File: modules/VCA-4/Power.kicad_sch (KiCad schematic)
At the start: 33 parts, among them J17 Conn_Eurorack_10, U1 LM4040, U2 SSI2164, U3 TL074, U4 TL074, U5 TL074, U6 TL074

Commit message: VCA-4: wip
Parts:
- removed R2: 150K, -lmp-misc:R_Axial_DIN0207_L6.3mm_D2.5mm_P7.62mm_Horizontal, symbol -lmp:R_1%_0W166
- removed R3: 100K, -lmp-misc:R_Axial_DIN0207_L6.3mm_D2.5mm_P7.62mm_Horizontal, symbol -lmp:R_1%_0W166
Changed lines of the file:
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@@
   (junction (at 67.31 107.95) (diameter 0) (color 0 0 0 0)
   )
-  (junction (at 78.74 49.53) (diameter 0) (color 0 0 0 0)
-  )
   (junction (at 57.15 57.15) (diameter 0) (color 0 0 0 0)
   )
@@
   (junction (at 92.71 107.95) (diameter 0) (color 0 0 0 0)
   )
-  (junction (at 87.63 41.91) (diameter 0) (color 0 0 0 0)
-  )
-  (junction (at 102.87 41.91) (diameter 0) (color 0 0 0 0)
-  )
   (junction (at 57.15 41.91) (diameter 0) (color 0 0 0 0)
   )
@@
     (stroke (width 0) (type default) (color 0 0 0 0))
   )
-  (wire (pts (xy 87.63 41.91) (xy 93.98 41.91))
-    (stroke (width 0) (type default) (color 0 0 0 0))
-  )
   (wire (pts (xy 199.39 102.87) (xy 204.47 102.87))
     (stroke (width 0) (type default) (color 0 0 0 0))
@@
     (stroke (width 0) (type default) (color 0 0 0 0))
   )
-  (wire (pts (xy 102.87 41.91) (xy 102.87 39.37))
-    (stroke (width 0) (type default) (color 0 0 0 0))
-  )
   (wire (pts (xy 140.97 107.95) (xy 163.83 107.95))
     (stroke (width 0) (type default) (color 0 0 0 0))
@@
     (stroke (width 0) (type default) (color 0 0 0 0))
   )
-  (wire (pts (xy 102.87 39.37) (xy 104.14 39.37))
-    (stroke (width 0) (type default) (color 0 0 0 0))
-  )
   (wire (pts (xy 139.7 105.41) (xy 140.97 105.41))
     (stroke (width 0) (type default) (color 0 0 0 0))
@@
     (stroke (width 0) (type default) (color 0 0 0 0))
   )
-  (wire (pts (xy 78.74 49.53) (xy 102.87 49.53))
-    (stroke (width 0) (type default) (color 0 0 0 0))
-  )
   (wire (pts (xy 57.15 41.91) (xy 63.5 41.91))
     (stroke (width 0) (type default) (color 0 0 0 0))
@@
   )
   (wire (pts (xy 38.1 46.99) (xy 38.1 49.53))
-    (stroke (width 0) (type default) (color 0 0 0 0))
-  )
-  (wire (pts (xy 102.87 41.91) (xy 101.6 41.91))
     (stroke (width 0) (type default) (color 0 0 0 0))
   )
@@
   (text "Hardware" (at 161.29 27.94 0)
     (effects (font (size 1.27 1.27) (thickness 0.254) bold) (justify left bottom))
-  )
-  (global_label "+2VREF" (shape output) (at 104.14 39.37 0) (fields_autoplaced)
-    (effects (font (size 1.27 1.27)) (justify left))
-    (property "Intersheet References" "${INTERSHEET_REFS}" (id 0) (at 1.27 0 0)
-      (effects (font (size 1.27 1.27)) hide)
-    )
   )
   (symbol (lib_id "-lmp-synth:Conn_Eurorack_Pwr_10") (at 43.18 46.99 0) (unit 1)
@@
     (pin "2")
   )
-  (symbol (lib_id "-lmp:R_1%_0W166") (at 102.87 45.72 0) (unit 1)
-    (in_bom yes) (on_board yes)
-    (property "Reference" "R3" (id 0) (at 104.648 44.5516 0)
-      (effects (font (size 1.27 1.27)) (justify left))
-    )
-    (property "Value" "100K" (id 1) (at 104.648 46.863 0)
-      (effects (font (size 1.27 1.27)) (justify left))
-    )
-    (property "Footprint" "-lmp-misc:R_Axial_DIN0207_L6.3mm_D2.5mm_P7.62mm_Horizontal" (id 2) (at 101.092 45.72 90)
-      (effects (font (size 1.27 1.27)) hide)
-    )
-    (property "Datasheet" "https://www.mouser.ca/datasheet/2/447/Yageo_LR_MFR_1-1714151.pdf" (id 3) (at 102.87 45.72 0)
-      (effects (font (size 1.27 1.27)) hide)
-    )
-    (property "Manufacturer" "YAGEO" (id 4) (at 102.87 45.72 0)
-      (effects (font (size 1.27 1.27)) hide)
-    )
-    (property "ManufacturerPartNum" "MFR-12*" (id 5) (at 102.87 45.72 0)
-      (effects (font (size 1.27 1.27)) hide)
-    )
-    (property "Distributor" "Mouser" (id 6) (at 102.87 45.72 0)
-      (effects (font (size 1.27 1.27)) hide)
-    )
-    (property "DistributorPartNum" "603-MFR-12*" (id 7) (at 102.87 45.72 0)
-      (effects (font (size 1.27 1.27)) hide)
-    )
-    (property "DistributorPartLink" "https://www.mouser.ca/c/?m=YAGEO&power+rating=166+mW+(1%2f6+W)&tolerance=1+%25&instock=y" (id 8) (at 102.87 45.72 0)
-      (effects (font (size 1.27 1.27)) hide)
-    )
-    (property "Value2" "1%, 1/6 W" (id 9) (at 107.823 45.72 90)
-      (effects (font (size 1.27 1.27)) hide)
-    )
-    (pin "1")
-    (pin "2")
-  )
   (symbol (lib_id "-lmp:R_1%_0W166") (at 72.39 41.91 270) (unit 1)
     (in_bom yes) (on_board yes)
@@
       (effects (font (size 1.27 1.27)) hide)
     )
-    (pin "1")
-    (pin "2")
-  )
-  (symbol (lib_id "-lmp:R_1%_0W166") (at 97.79 41.91 270) (unit 1)
-    (in_bom yes) (on_board yes)
-    (property "Reference" "R2" (id 0) (at 97.79 36.6522 90))
-    (property "Value" "150K" (id 1) (at 97.79 38.9636 90))
-    (property "Footprint" "-lmp-misc:R_Axial_DIN0207_L6.3mm_D2.5mm_P7.62mm_Horizontal" (id 2) (at 97.79 40.132 90)
-      (effects (font (size 1.27 1.27)) hide)
-    )
-    (property "Datasheet" "https://www.mouser.ca/datasheet/2/447/Yageo_LR_MFR_1-1714151.pdf" (id 3) (at 97.79 41.91 0)
-      (effects (font (size 1.27 1.27)) hide)
-    )
-    (property "Manufacturer" "YAGEO" (id 4) (at 97.79 41.91 0)
-      (effects (font (size 1.27 1.27)) hide)
-    )
-    (property "ManufacturerPartNum" "MFR-12*" (id 5) (at 97.79 41.91 0)
-      (effects (font (size 1.27 1.27)) hide)
-    )
-    (property "Distributor" "Mouser" (id 6) (at 97.79 41.91 0)
-      (effects (font (size 1.27 1.27)) hide)
-    )
-    (property "DistributorPartNum" "603-MFR-12*" (id 7) (at 97.79 41.91 0)
-      (effects (font (size 1.27 1.27)) hide)
-    )
-    (property "DistributorPartLink" "https://www.mouser.ca/c/?m=YAGEO&power+rating=166+mW+(1%2f6+W)&tolerance=1+%25&instock=y" (id 8) (at 97.79 41.91 0)
-      (effects (font (size 1.27 1.27)) hide)
-    )
-    (property "Value2" "1%, 1/6 W" (id 9) (at 97.79 46.863 90)
-      (effects (font (size 1.27 1.27)) hide)
-    )

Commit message: VCA-4: wip
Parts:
- U2: footprint -lmp-breakout:Breakout_DIP-16_W15.24mm -> -lmp-breakout:Breakout_DIP-SOIC-16_W15.24mm
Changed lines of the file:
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@@
       (effects (font (size 1.27 1.27)) (justify left))
     )
-    (property "Footprint" "-lmp-breakout:Breakout_DIP-16_W15.24mm" (id 2) (at 149.86 111.76 0)
+    (property "Footprint" "-lmp-breakout:Breakout_DIP-SOIC-16_W15.24mm" (id 2) (at 149.86 111.76 0)
       (effects (font (size 1.27 1.27)) hide)
     )

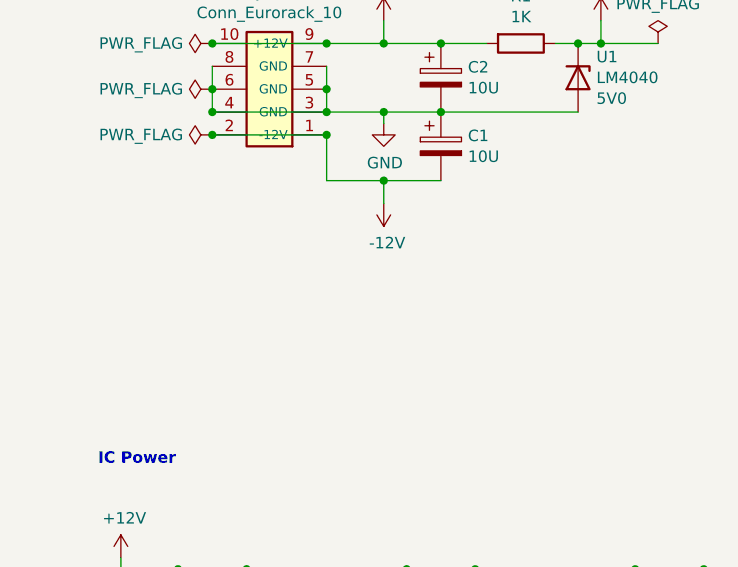
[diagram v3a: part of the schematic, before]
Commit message: VCA4: Add Eurorack power cable to BOM
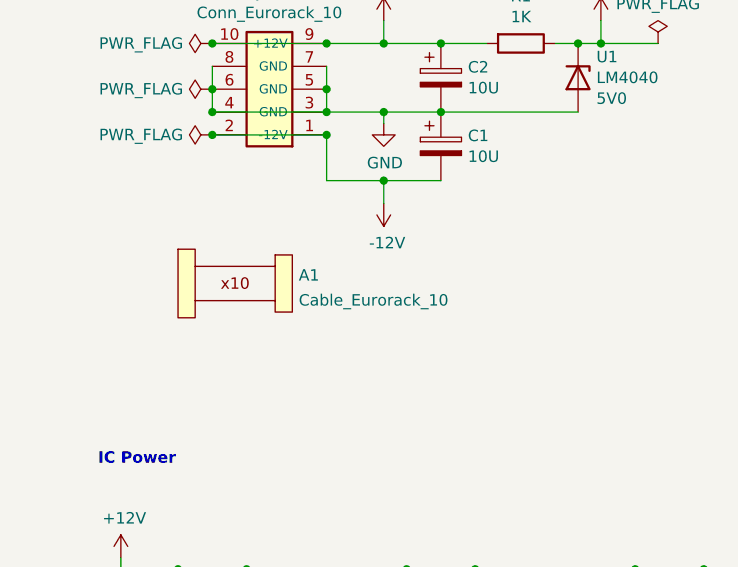
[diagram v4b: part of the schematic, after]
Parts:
- added A1: Cable_Eurorack_10, -lmp-misc:NoFootprint, symbol -lmp-synth:Cable_Eurorack_10
- U3, U4, U5, U6: footprint -lmp-misc:DIP-14_W7.62mm_LongPads -> Package_DIP:DIP-14_W7.62mm
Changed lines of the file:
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@@
       (effects (font (size 1.27 1.27)) (justify left))
     )
-    (property "Footprint" "-lmp-misc:DIP-14_W7.62mm_LongPads" (id 2) (at 35.56 105.41 0)
+    (property "Footprint" "Package_DIP:DIP-14_W7.62mm" (id 2) (at 35.56 105.41 0)
       (effects (font (size 1.27 1.27)) hide)
     )
@@
       (effects (font (size 1.27 1.27)) (justify left))
     )
-    (property "Footprint" "-lmp-misc:DIP-14_W7.62mm_LongPads" (id 2) (at 60.96 105.41 0)
+    (property "Footprint" "Package_DIP:DIP-14_W7.62mm" (id 2) (at 60.96 105.41 0)
       (effects (font (size 1.27 1.27)) hide)
     )
@@
       (effects (font (size 1.27 1.27)) (justify left))
     )
-    (property "Footprint" "-lmp-misc:DIP-14_W7.62mm_LongPads" (id 2) (at 86.36 105.41 0)
+    (property "Footprint" "Package_DIP:DIP-14_W7.62mm" (id 2) (at 86.36 105.41 0)
       (effects (font (size 1.27 1.27)) hide)
     )
@@
     (property "Reference" "U6" (id 0) (at 212.09 96.0882 0))
     (property "Value" "TL074" (id 1) (at 212.09 98.3996 0))
-    (property "Footprint" "-lmp-misc:DIP-14_W7.62mm_LongPads" (id 2) (at 210.82 102.87 0)
+    (property "Footprint" "Package_DIP:DIP-14_W7.62mm" (id 2) (at 210.82 102.87 0)
       (effects (font (size 1.27 1.27)) hide)
     )
@@
       (effects (font (size 1.27 1.27)) (justify left))
     )
-    (property "Footprint" "-lmp-misc:DIP-14_W7.62mm_LongPads" (id 2) (at 111.76 105.41 0)
+    (property "Footprint" "Package_DIP:DIP-14_W7.62mm" (id 2) (at 111.76 105.41 0)
       (effects (font (size 1.27 1.27)) hide)
     )
@@
     (pin "2")
   )
+  (symbol (lib_id "-lmp-synth:Cable_Eurorack_10") (at 40.64 68.58 0) (unit 1)
+    (in_bom yes) (on_board no) (fields_autoplaced)
+    (property "Reference" "A1" (id 0) (at 47.7012 67.6715 0)
+      (effects (font (size 1.27 1.27)) (justify left))
+    )
+    (property "Value" "Cable_Eurorack_10" (id 1) (at 47.7012 70.4466 0)
+      (effects (font (size 1.27 1.27)) (justify left))
+    )
+    (property "Footprint" "-lmp-misc:NoFootprint" (id 2) (at 41.275 73.66 0)
+      (effects (font (size 1.27 1.27)) hide)
+    )
+    (property "Datasheet" "" (id 3) (at 40.64 60.325 0)
+      (effects (font (size 1.27 1.27)) hide)
+    )
+    (property "Note" "Length as required" (id 4) (at 40.64 71.12 0)
+      (effects (font (size 1.27 1.27)) hide)
+    )
+    (property "Distributor" "Thonk" (id 5) (at 40.64 73.66 0)
+      (effects (font (size 1.27 1.27)) hide)
+    )
+    (property "DistributorPartLink" "https://www.thonk.co.uk/shop/eurorack-power-cables/" (id 6) (at 40.64 73.66 0)
+      (effects (font (size 1.27 1.27)) hide)
+    )
+    (property "Distributor2" "SynthCube" (id 7) (at 40.64 73.66 0)
+      (effects (font (size 1.27 1.27)) hide)
+    )
+    (property "DistributorPartLink2" "https://synthcube.com/cart/eurorack-ribbon-power-cables" (id 8) (at 40.64 73.66 0)
+      (effects (font (size 1.27 1.27)) hide)
+    )
+    (property "Distributor3" "Modular Addict" (id 9) (at 40.64 73.66 0)
+      (effects (font (size 1.27 1.27)) hide)
+    )
+    (property "DistributorPartLink3" "https://modularaddict.com/parts/eurorack-power-cables-1" (id 10) (at 40.64 73.66 0)
+      (effects (font (size 1.27 1.27)) hide)
+    )
+  )
   (symbol (lib_id "-lmp-synth:HW_Standoff_F-F_11mm_M3x0.50") (at 203.2 49.53 0) (unit 1)

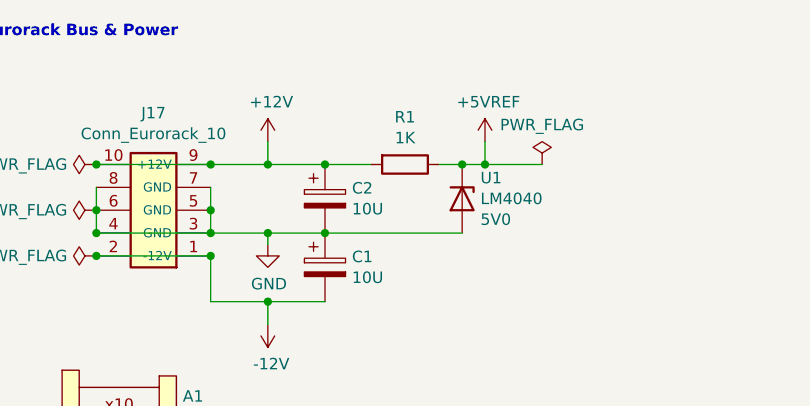
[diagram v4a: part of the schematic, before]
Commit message: VCA-4: BOM cleanup
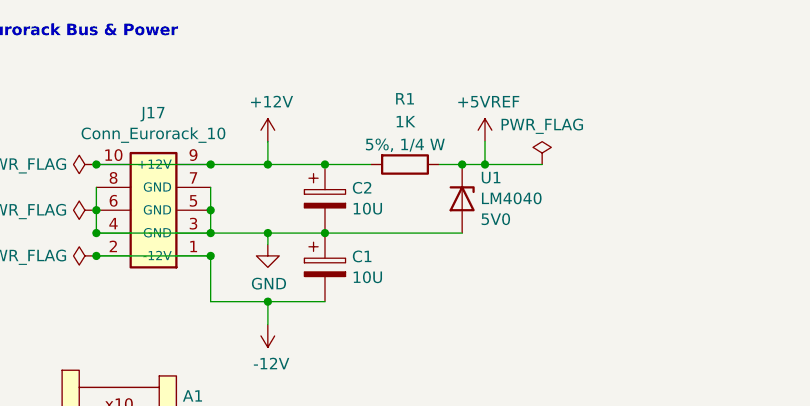
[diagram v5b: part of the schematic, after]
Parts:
- R1: footprint -lmp-misc:R_Axial_DIN0207_L6.3mm_D2.5mm_P7.62mm_Horizontal -> -lmp-misc:R_Axial_DIN0207_L6.3mm_D2.5mm_P10.16mm_Horizontal; symbol -lmp:R_1%_0W166 -> -lmp-synth:R_1K_Output; DistributorPartLink https://www.mouser.ca/c/?m=YAGEO&power+rating=166+mW+(1%2f6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 -> https://www.mouser.ca/ProductDetail/Vishay-Dale/CCF071K00JK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; DistributorPartNum 603-MFR-12* -> 71-CCF071K00JKE36; Manufacturer YAGEO -> Vishay / Dale; ManufacturerPartNum MFR-12* -> CCF071K00JKE36; Note (none) -> Output limiting; Value2 1%, 1/6 W -> 5%, 1/4 W
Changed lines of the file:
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@@
     (pin "2")
   )
-  (symbol (lib_id "-lmp:R_1%_0W166") (at 72.39 41.91 270) (unit 1)
-    (in_bom yes) (on_board yes)
-    (property "Reference" "R1" (id 0) (at 72.39 36.6522 90))
-    (property "Value" "1K" (id 1) (at 72.39 38.9636 90))
-    (property "Footprint" "-lmp-misc:R_Axial_DIN0207_L6.3mm_D2.5mm_P7.62mm_Horizontal" (id 2) (at 72.39 40.132 90)
+  (symbol (lib_id "-lmp-synth:R_1K_Output") (at 72.39 41.91 270) (unit 1)
+    (in_bom yes) (on_board yes) (fields_autoplaced)
+    (property "Reference" "R1" (id 0) (at 72.39 34.6574 90))
+    (property "Value" "1K" (id 1) (at 72.39 37.1943 90))
+    (property "Footprint" "-lmp-misc:R_Axial_DIN0207_L6.3mm_D2.5mm_P10.16mm_Horizontal" (id 2) (at 72.39 40.132 90)
       (effects (font (size 1.27 1.27)) hide)
     )
-    (property "Datasheet" "https://www.mouser.ca/datasheet/2/447/Yageo_LR_MFR_1-1714151.pdf" (id 3) (at 72.39 41.91 0)
+    (property "Datasheet" "https://www.mouser.ca/datasheet/2/427/ccf07-1762725.pdf" (id 3) (at 72.39 41.91 0)
       (effects (font (size 1.27 1.27)) hide)
     )
-    (property "Manufacturer" "YAGEO" (id 4) (at 72.39 41.91 0)
+    (property "Manufacturer" "Vishay / Dale" (id 4) (at 72.39 41.91 0)
       (effects (font (size 1.27 1.27)) hide)
     )
-    (property "ManufacturerPartNum" "MFR-12*" (id 5) (at 72.39 41.91 0)
+    (property "ManufacturerPartNum" "CCF071K00JKE36" (id 5) (at 72.39 41.91 0)
       (effects (font (size 1.27 1.27)) hide)
     )
-    (property "Distributor" "Mouser" (id 6) (at 72.39 41.91 0)
+    (property "Distributor" "Mouser" (id 6) (at 72.39 40.005 90)
       (effects (font (size 1.27 1.27)) hide)
     )
-    (property "DistributorPartNum" "603-MFR-12*" (id 7) (at 72.39 41.91 0)
+    (property "DistributorPartNum" "71-CCF071K00JKE36" (id 7) (at 72.39 41.91 0)
       (effects (font (size 1.27 1.27)) hide)
     )
-    (property "DistributorPartLink" "https://www.mouser.ca/c/?m=YAGEO&power+rating=166+mW+(1%2f6+W)&tolerance=1+%25&instock=y" (id 8) (at 72.39 41.91 0)
+    (property "DistributorPartLink" "https://www.mouser.ca/ProductDetail/Vishay-Dale/CCF071K00JKE36?qs=sGAEpiMZZMsPqMdJzcrNwqw41JD0NFylHV1MADcQnpo%3D" (id 8) (at 72.39 41.91 0)
       (effects (font (size 1.27 1.27)) hide)
     )
-    (property "Value2" "1%, 1/6 W" (id 9) (at 72.39 46.863 90)
+    (property "Value2" "5%, 1/4 W" (id 9) (at 72.39 39.7312 90))
+    (property "Note" "Output limiting" (id 10) (at 70.485 40.005 90)
       (effects (font (size 1.27 1.27)) hide)
     )

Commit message: VCA-4: PCB tweaks
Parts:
- C1, C2: footprint -lmp-misc:CP_Radial_D5.0mm_P2.50mm -> -lmp-misc:CP_Radial_D4.0mm_P1.50mm
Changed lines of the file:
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@@
       (effects (font (size 1.27 1.27)) (justify left))
     )
-    (property "Footprint" "-lmp-misc:CP_Radial_D5.0mm_P2.50mm" (id 2) (at 64.4652 49.53 0)
+    (property "Footprint" "-lmp-misc:CP_Radial_D4.0mm_P1.50mm" (id 2) (at 64.4652 49.53 0)
       (effects (font (size 1.27 1.27)) hide)
     )
@@
       (effects (font (size 1.27 1.27)) (justify left))
     )
-    (property "Footprint" "-lmp-misc:CP_Radial_D5.0mm_P2.50mm" (id 2) (at 64.4652 57.15 0)
+    (property "Footprint" "-lmp-misc:CP_Radial_D4.0mm_P1.50mm" (id 2) (at 64.4652 57.15 0)
       (effects (font (size 1.27 1.27)) hide)
     )

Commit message: VCA-4: schematic tweaks
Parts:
- H1, H10, H5, H6: value HW_Screw_M3x0.50x6 -> Screw_M3x0.50x6
- H3, H8: value HW_Standoff_F-F_11mm_M3x0.50 -> Standoff_F-F_11mm_M3x0.50
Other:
- title: Power - Eurorack 4XVCA Module -> Power & Hardware - Eurorack 4XVCA Module
- moved on the sheet: A1, C10, C11, C12, C3, C4, C5, C6, C7, C8, C9, R4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

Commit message: VCA-4: BOM update
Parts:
- J17: Distributor2 (none) -> Mouser; DistributorPartLink2 (none) -> https://www.mouser.ca/ProductDetail/523-G821EU210AAL10Y; DistributorPartNum2 (none) -> 523-G821EU210AAL10Y
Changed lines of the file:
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@@
+      (effects (font (size 1.27 1.27)) hide)
+    )
+    (property "Distributor2" "Mouser" (id 9) (at 43.18 46.99 0)
+      (effects (font (size 1.27 1.27)) hide)
+    )
+    (property "DistributorPartNum2" "523-G821EU210AAL10Y" (id 10) (at 43.18 46.99 0)
+      (effects (font (size 1.27 1.27)) hide)
+    )
+    (property "DistributorPartLink2" "https://www.mouser.ca/ProductDetail/523-G821EU210AAL10Y" (id 11) (at 43.18 46.99 0)
       (effects (font (size 1.27 1.27)) hide)
     )
